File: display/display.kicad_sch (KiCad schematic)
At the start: 17 parts, among them J1 Conn, J2 KEYAB, U1 MAN74A, U2 MAN74A, U3 AS1115-BSST, U4 MAN74A, U5 MAN74A, U6 MAN74A

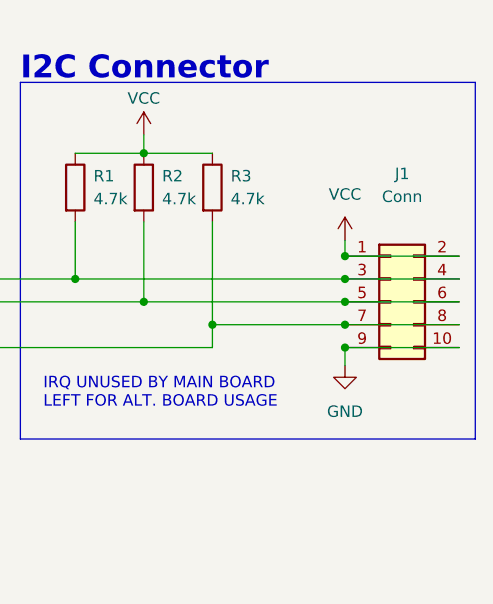
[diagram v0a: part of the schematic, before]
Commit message: Added initial code base, improved and fixed hardware up to Rev 1.5/1.2 for the main and display boards respectively, and add pictures of (mostly) complete result
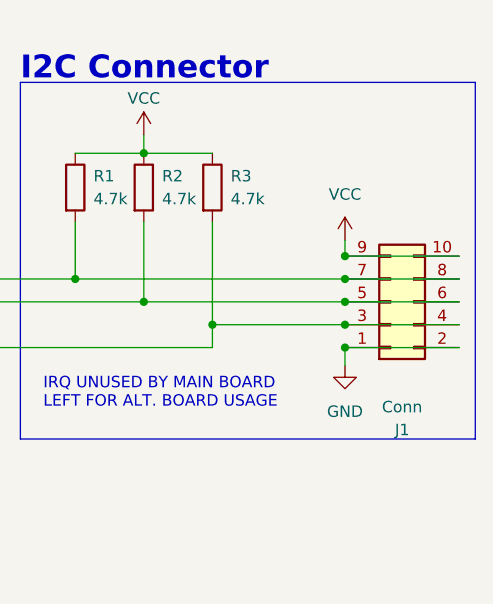
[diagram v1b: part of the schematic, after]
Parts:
- J1: footprint personal:DISPIO10 -> Connector_PinHeader_2.54mm:PinHeader_2x05_P2.54mm_Horizontal
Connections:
- net GND: now also J1.1 (Pin_1), J1.2 (Pin_2); no longer J1.10 (Pin_10), J1.9 (Pin_9)
- net VCC: now also J1.10 (Pin_10), J1.9 (Pin_9); no longer J1.1 (Pin_1), J1.2 (Pin_2)
- net at R1.2, U3.14 (SCL): now also J1.7 (Pin_7), J1.8 (Pin_8); no longer J1.3 (Pin_3), J1.4 (Pin_4)
- net at R3.2, U3.24 (IRQ): now also J1.3 (Pin_3), J1.4 (Pin_4); no longer J1.7 (Pin_7), J1.8 (Pin_8)
